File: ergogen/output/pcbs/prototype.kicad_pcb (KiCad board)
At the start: 2 copper layers, 136.1 x 97.6 mm, 44 parts

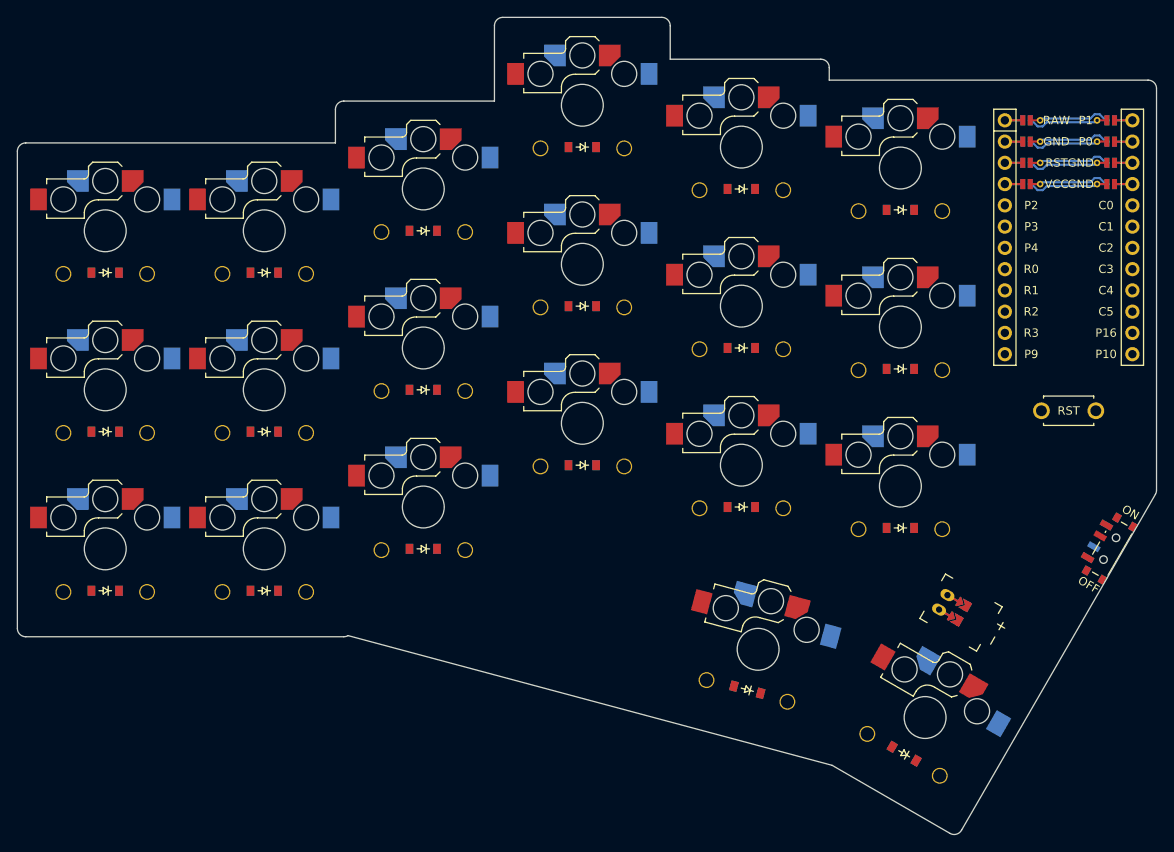
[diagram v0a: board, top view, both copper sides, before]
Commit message: feat: mounting holes
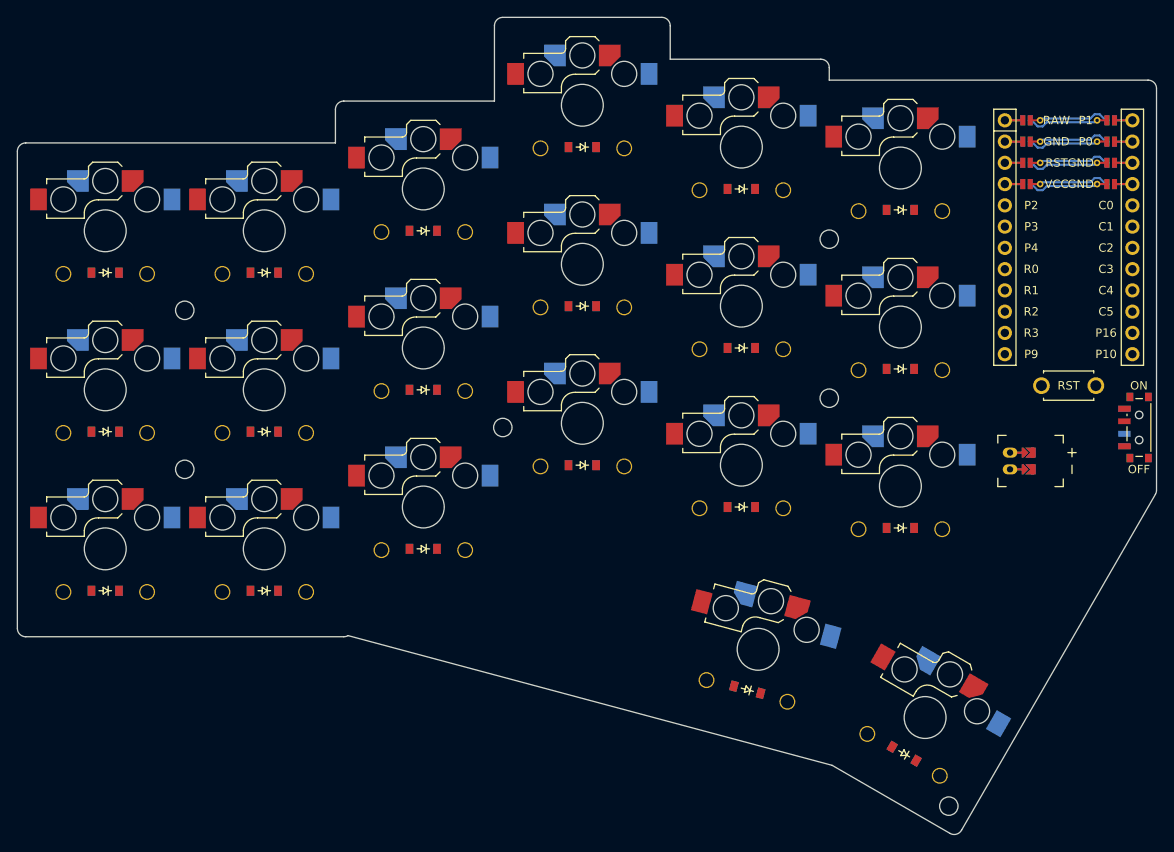
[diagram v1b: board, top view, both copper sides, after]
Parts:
- added MH1: , ceoloide:mounting_hole_npth, F.Cu at (109.5, 90.5)
- added MH2: , ceoloide:mounting_hole_npth, F.Cu at (109.5, 71.5)
- added MH3: , ceoloide:mounting_hole_npth, F.Cu at (186.5, 82.0)
- added MH4: , ceoloide:mounting_hole_npth, F.Cu at (186.5, 63.0)
- added MH5: , ceoloide:mounting_hole_npth, F.Cu at (200.8, 130.7)
- added MH6: , ceoloide:mounting_hole_npth, F.Cu at (147.5, 85.5)
- moved JST1 18.7 mm to (208.1, 89.5), turned to 90 degrees
- moved PWR1 14.9 mm to (223.5, 85.5), turned to 0 degrees
- moved RST1 3.00 mm to (215.1, 80.5)

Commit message: feat: updated footprints, suggestions
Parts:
- removed MH5, MH6: , ceoloide:mounting_hole_npth
- moved MCU1 1.00 mm to (215.1, 60.5)
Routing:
- net C5: track 0.00 -> 33.1 mm, vias 0 -> 4
- net C4: track 0.00 -> 33.1 mm, vias 0 -> 4
- net C1: track 0.00 -> 24.8 mm, vias 0 -> 3
- net C0: track 0.00 -> 24.8 mm, vias 0 -> 3
- net C3: track 0.00 -> 24.8 mm, vias 0 -> 3
- net C2: track 0.00 -> 24.8 mm, vias 0 -> 3
- net pinky_top: track 0.00 -> 19.1 mm, vias 0 -> 1
- net pinky_home: track 0.00 -> 19.1 mm, vias 0 -> 1
- net pinky_bottom: track 0.00 -> 19.1 mm, vias 0 -> 1
- net outer_top: track 0.00 -> 19.1 mm, vias 0 -> 1
- net outer_home: track 0.00 -> 19.1 mm, vias 0 -> 1
- net outer_bottom: track 0.00 -> 19.1 mm, vias 0 -> 1
- net ring_top: track 0.00 -> 19.1 mm, vias 0 -> 1
- net ring_home: track 0.00 -> 19.1 mm, vias 0 -> 1
- net ring_bottom: track 0.00 -> 19.1 mm, vias 0 -> 1
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
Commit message: feat: routing, silkscreen
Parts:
- added LOGO1: , ceoloide:utility_ergogen_logo, F.Cu at (157.0, 104.0)
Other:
- board text added: "JLCJLCJLCJLCJLCJLC"
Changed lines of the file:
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@@
   (title_block
     (title "prototype")
-    (date "2024-12-02")
+    (date "2024-12-04")
     (rev "v1.0.0")
     (company "Unknown")
@@
     )
   )
+  (gr_text "JLCJLCJLCJLCJLCJLC"
+    (at 215.1 67.5 90)
+    (layer "F.SilkS" )
+    (effects
+      (font
+        (size 1 1)
+        (thickness 0.15)
+      )
+    )
+  )
+  (gr_text "JLCJLCJLCJLCJLCJLC"
+    (at 215.1 67.5 90)
+    (layer "B.SilkS" )
+    (effects
+      (font
+        (size 1 1)
+        (thickness 0.15)
+      )
+      (justify  mirror)
+    )
+  )
+  (footprint "ceoloide:utility_ergogen_logo"
+    (layer "F.Cu")
+    (at 157 104 0)
+    (property "Reference" "LOGO1"
+      (at 11.43 0 0)
+      (layer "F.Fab")
+      hide
+      (effects (font (size 1 1) (thickness 0.15)))
+    )
+		(attr exclude_from_pos_files exclude_from_bom)
+    (fp_poly
+      (pts
+          (xy 6.253078 0.000000) (xy 6.253078 6.253078) (xy 0.000000 6.253078) (xy -6.253075 6.253078) (xy -6.253075 2.532720)
+          (xy -4.345887 2.532720) (xy -0.054713 2.524792) (xy 4.236460 2.516865) (xy 4.244763 1.657068) (xy 4.253063 0.797268)
+          (xy 3.822275 1.227167) (xy 3.391485 1.657068) (xy -0.477200 1.657068) (xy -4.345887 1.657068) (xy -4.345887 2.094892)
+          (xy -4.345887 2.532720) (xy -6.253075 2.532720) (xy -6.253075 0.375185) (xy -3.485253 0.375185) (xy -1.593695 0.375185)
+          (xy 0.297860 0.375185) (xy 0.734738 -0.062530) (xy 1.171615 -0.500245) (xy -0.719940 -0.500245) (xy -2.611498 -0.500245)
+          (xy -3.048375 -0.062530) (xy -3.485253 0.375185) (xy -6.253075 0.375185) (xy -6.253075 0.000000) (xy -6.253075 -2.657558)
+          (xy -4.345887 -2.657558) (xy -4.345887 -2.219842) (xy -4.345887 -1.782125) (xy -0.476362 -1.782125) (xy 3.393165 -1.782125)
+          (xy 3.814377 -1.360043) (xy 3.945855 -1.228708) (xy 4.061438 -1.114035) (xy 4.154197 -1.022833) (xy 4.217212 -0.961908)
+          (xy 4.243555 -0.938065) (xy 4.243843 -0.937960) (xy 4.245997 -0.967895) (xy 4.247942 -1.052380) (xy 4.249600 -1.183430)
+          (xy 4.250897 -1.353062) (xy 4.251753 -1.553300) (xy 4.252090 -1.776157) (xy 4.252092 -1.797758) (xy 4.252092 -2.657558)
+          (xy -0.046898 -2.657558) (xy -4.345887 -2.657558) (xy -6.253075 -2.657558) (xy -6.253075 -6.253075) (xy 0.000000 -6.253075)
+          (xy 6.253078 -6.253075)
+      )
+			(stroke
+				(width 0.01)
+				(type solid)
+			)
+			(fill solid)
+      (layer "F.SilkS")
+    )
+    (fp_poly
+      (pts
+          (xy -6.253078 0.000000) (xy -6.253078 6.253078) (xy 0.000000 6.253078) (xy 6.253075 6.253078) (xy 6.253075 2.532720)
+          (xy 4.345887 2.532720) (xy 0.054713 2.524792) (xy -4.236460 2.516865) (xy -4.244763 1.657068) (xy -4.253063 0.797268)
+          (xy -3.822275 1.227167) (xy -3.391485 1.657068) (xy 0.477200 1.657068) (xy 4.345887 1.657068) (xy 4.345887 2.094892)
+          (xy 4.345887 2.532720) (xy 6.253075 2.532720) (xy 6.253075 0.375185) (xy 3.485253 0.375185) (xy 1.593695 0.375185)
+          (xy -0.297860 0.375185) (xy -0.734738 -0.062530) (xy -1.171615 -0.500245) (xy 0.719940 -0.500245) (xy 2.611498 -0.500245)
+          (xy 3.048375 -0.062530) (xy 3.485253 0.375185) (xy 6.253075 0.375185) (xy 6.253075 0.000000) (xy 6.253075 -2.657558)
+          (xy 4.345887 -2.657558) (xy 4.345887 -2.219842) (xy 4.345887 -1.782125) (xy 0.476362 -1.782125) (xy -3.393165 -1.782125)
+          (xy -3.814377 -1.360043) (xy -3.945855 -1.228708) (xy -4.061438 -1.114035) (xy -4.154197 -1.022833) (xy -4.217212 -0.961908)
+          (xy -4.243555 -0.938065) (xy -4.243843 -0.937960) (xy -4.245997 -0.967895) (xy -4.247942 -1.052380) (xy -4.249600 -1.183430)
+          (xy -4.250897 -1.353062) (xy -4.251753 -1.553300) (xy -4.252090 -1.776157) (xy -4.252092 -1.797758) (xy -4.252092 -2.657558)
+          (xy 0.046898 -2.657558) (xy 4.345887 -2.657558) (xy 6.253075 -2.657558) (xy 6.253075 -6.253075) (xy 0.000000 -6.253075)
+          (xy -6.253078 -6.253075)
+      )
+			(stroke
+				(width 0.01)
+				(type solid)
+			)
+			(fill solid)
+      (layer "B.SilkS")
+    )
+  )
